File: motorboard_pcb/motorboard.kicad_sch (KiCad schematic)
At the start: 3 parts, among them U1 XIAO-RP2350-SMD, U3 ISO1640BQDRQ1, U4 LM5012QDDARQ1

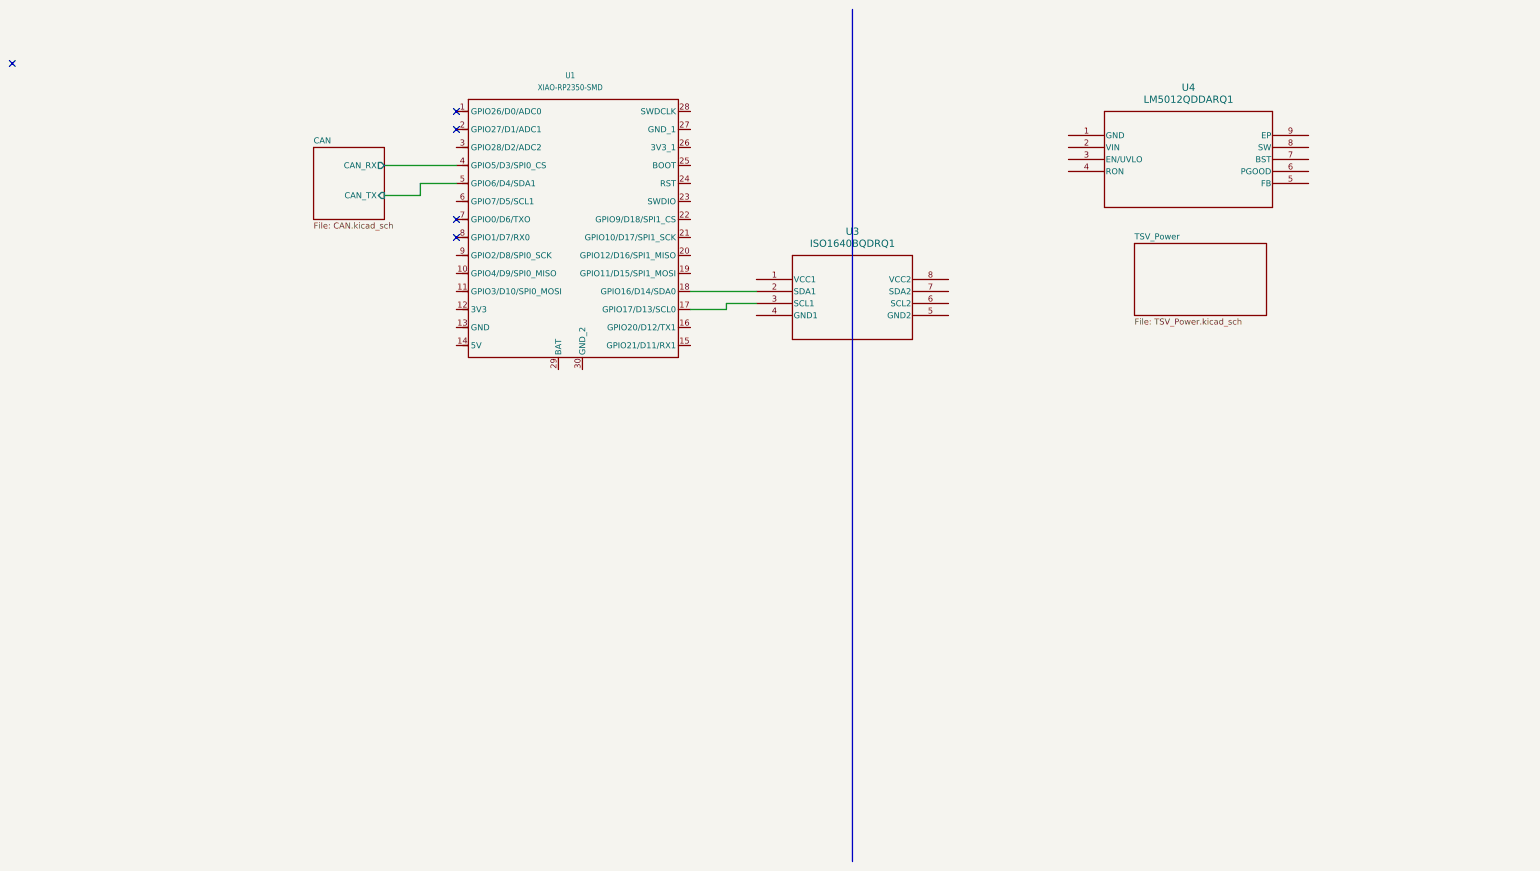
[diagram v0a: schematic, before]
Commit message: switch isolator for SPI, output stage (DAC, op amp)
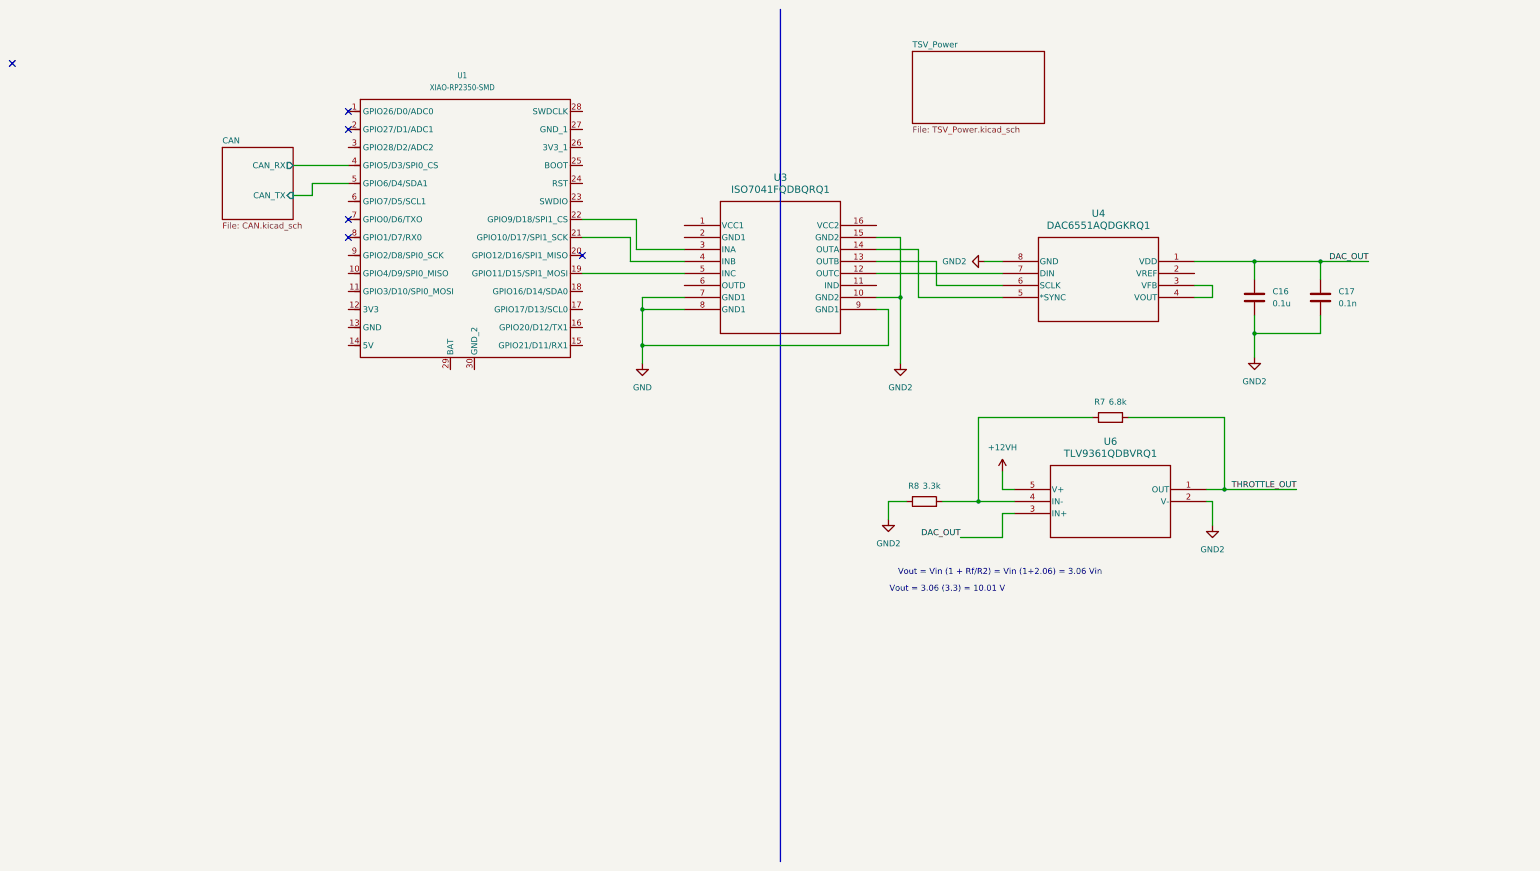
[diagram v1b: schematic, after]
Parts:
- removed U3: ISO1640BQDRQ1, ISO1640:SOIC8_D_TEX, symbol ISO1640:ISO1640BQDRQ1
- removed U4: LM5012QDDARQ1, SO-8-DDA_TEX, symbol 2025-02-28_21-05-36:LM5012QDDARQ1
- added C16: 0.1u, symbol Device:C
- added C17: 0.1n, symbol Device:C
- added R7: 6.8k, symbol Device:R
- added R8: 3.3k, symbol Device:R
- added U3: ISO7041FQDBQRQ1, SSOP16_DBQ_TEX, symbol ISO7041:ISO7041FQDBQRQ1
- added U4: DAC6551AQDGKRQ1, DGK8_TEX, symbol DAC6551:DAC6551AQDGKRQ1
- added U6: TLV9361QDBVRQ1, SOT23_DBV_TEX, symbol TLV9361:TLV9361QDBVRQ1
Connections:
- net at U1.19 (GPIO11/D15/SPI1_MOSI): now also U3.5 (INC)
- net at U1.21 (GPIO10/D17/SPI1_SCK): now also U3.4 (INB)
- net at U1.22 (GPIO9/D18/SPI1_CS): now also U3.3 (INA)
- new net: R7.1, R8.2, U6.4 (IN-)
- new net: U3.12 (OUTC), U4.7 (DIN)
- new net: U3.13 (OUTB), U4.6 (SCLK)
- new net: U3.14 (OUTA), U4.5 (*SYNC)
- new net: U4.3 (VFB), U4.4 (VOUT)
- new net +12VH: U6.5 (V+)
- new net DAC_OUT: C16.1, C17.1, U4.1 (VDD), U6.3 (IN+)
- new net GND: U3.7 (GND1), U3.8 (GND1), U3.9 (GND1)
- new net GND2: C16.2, C17.2, R8.1, U3.10 (GND2), U3.15 (GND2), U4.8 (GND), U6.2 (V-)
- new net THROTTLE_OUT: R7.2, U6.1 (OUT)
- no-connect marks 5 -> 6
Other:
- note added: "Vout = 3.06 (3.3) = 10.01 V"
- note added: "Vout = Vin (1 + Rf/R2) = Vin (1+2.06) = 3.06 Vin"
- moved on the sheet: U1

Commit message: Schematic done, pending review
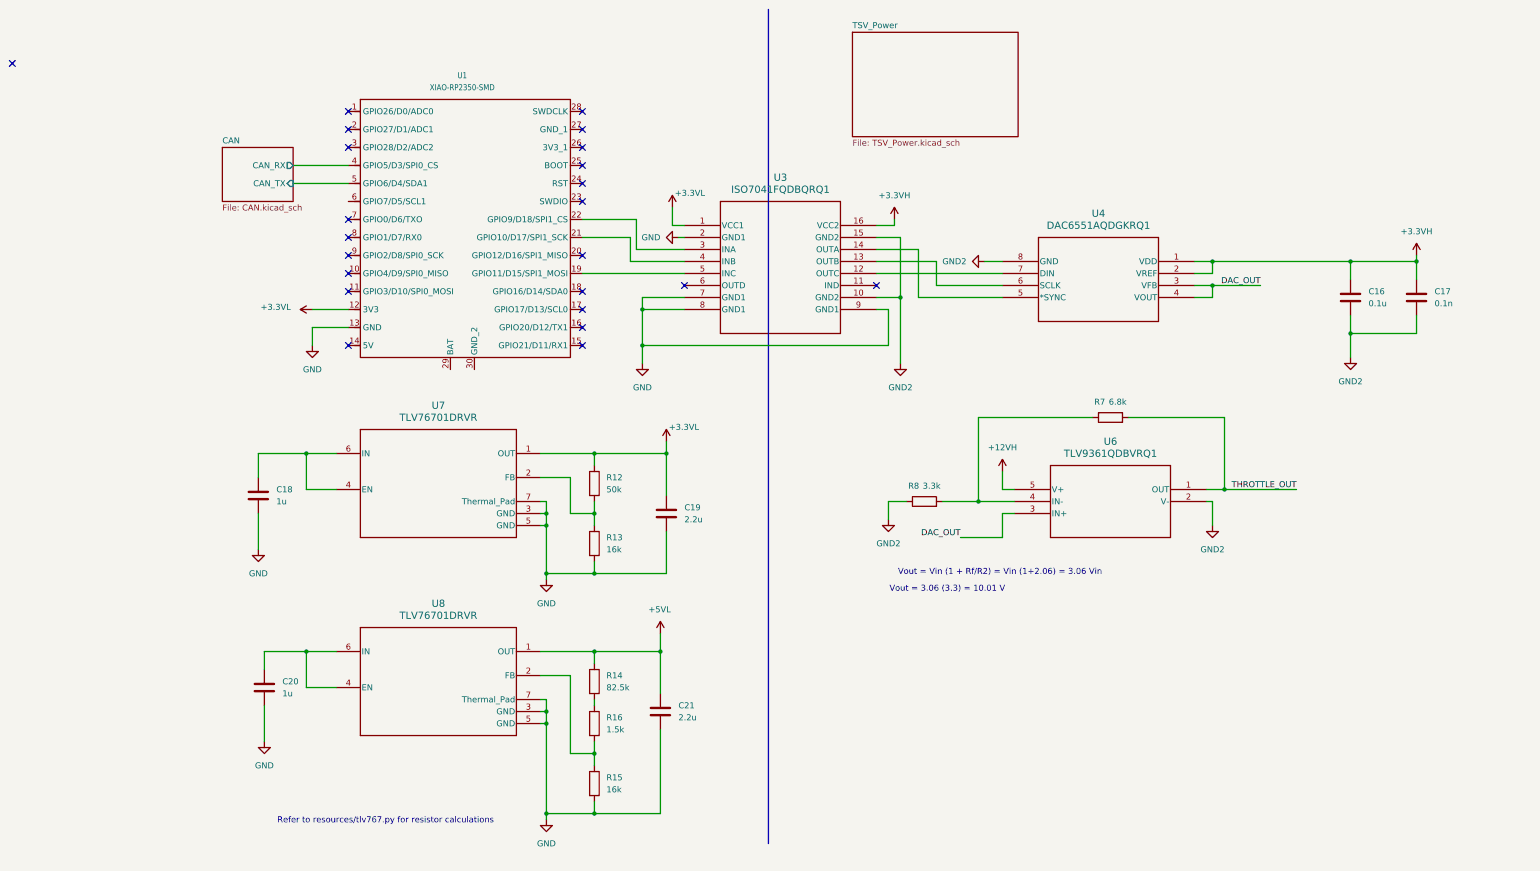
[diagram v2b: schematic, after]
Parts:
- added C18, C20: 1u, symbol Device:C
- added C19, C21: 2.2u, symbol Device:C
- added R12: 50k, symbol Device:R
- added R13, R15: 16k, symbol Device:R
- added R14: 82.5k, symbol Device:R
- added R16: 1.5k, symbol Device:R
- added U7, U8: TLV76701DRVR, TLV76701:DRV0006A-IPC_A, symbol TLV76701:TLV76701DRVR
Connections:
- net DAC_OUT: now also U4.3 (VFB), U4.4 (VOUT); no longer C16.1, C17.1, U4.1 (VDD)
- net GND: now also U1.13 (GND), U3.2 (GND1), C18.2, C19.2, C20.2, C21.2, R13.2, R15.2, U7.3 (GND), U7.5 (GND), U7.7 (Thermal_Pad), U8.3 (GND), U8.5 (GND), U8.7 (Thermal_Pad)
- net +3.3VL: now reaches U3.1 (VCC1)
- net +3.3VL: now also U1.12 (3V3), C19.1, R12.1, U7.1 (OUT)
- net +3.3VH: now reaches U3.16 (VCC2)
- net +3.3VH: now also C16.1, C17.1, U4.1 (VDD), U4.2 (VREF)
- new net: R15.1, R16.2, U8.2 (FB)
- new net: C20.1, U8.4 (EN), U8.6 (IN)
- new net: R12.2, R13.1, U7.2 (FB)
- new net: C18.1, U7.4 (EN), U7.6 (IN)
- new net: R14.2, R16.1
- new net +5VL: C21.1, R14.1, U8.1 (OUT)
- no-connect marks 6 -> 23
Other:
- note added: "Refer to resources/tlv767.py for resistor calculations"
- moved on the sheet: C16, C17

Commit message: Initial layout, all resistors/caps are 0602
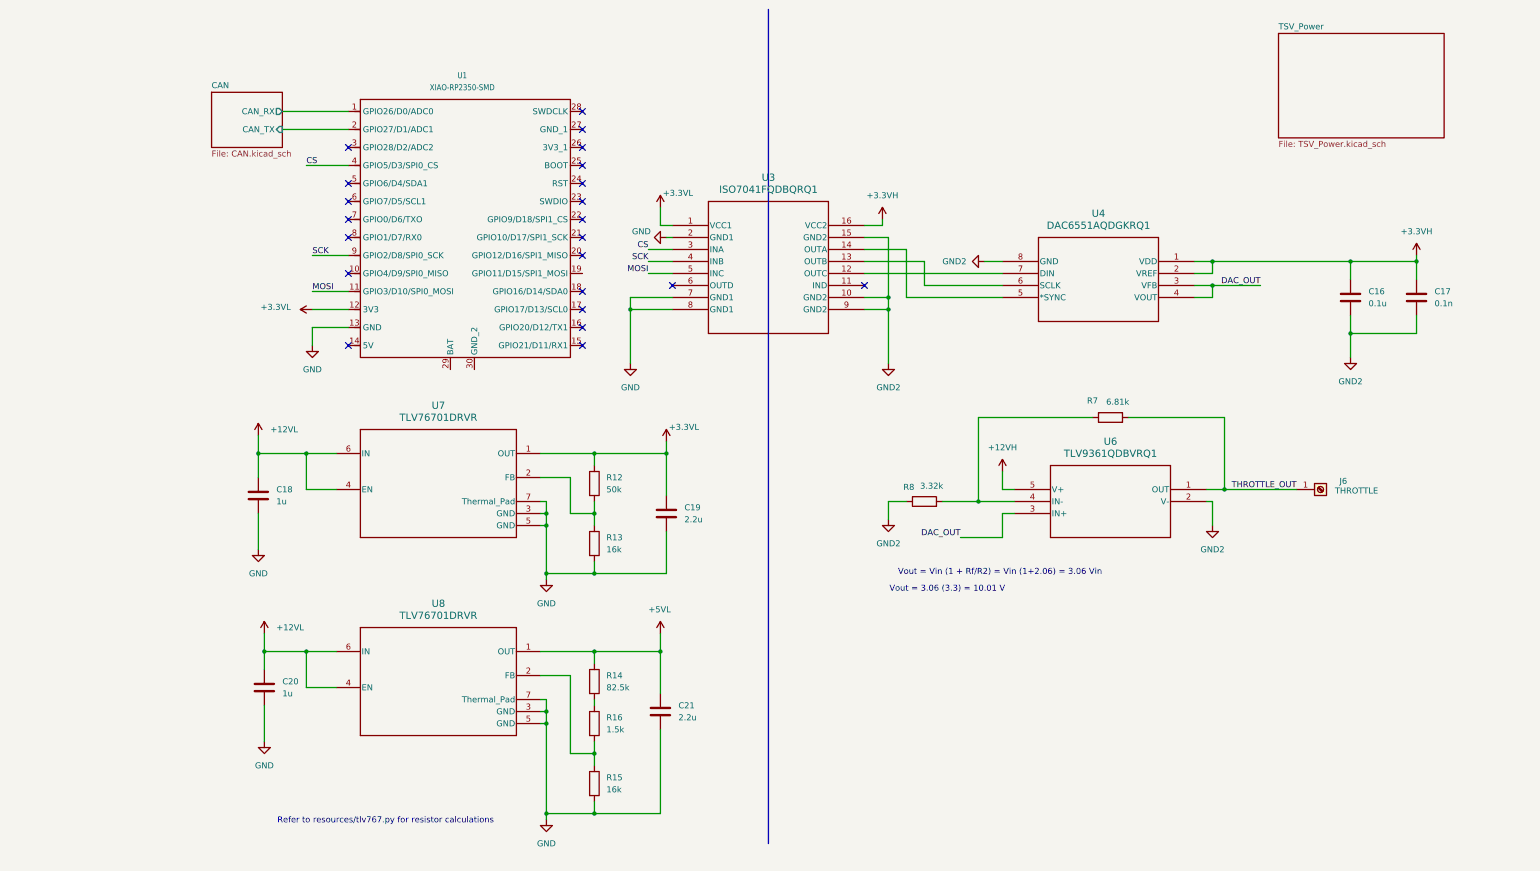
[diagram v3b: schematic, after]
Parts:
- added J6: THROTTLE, TerminalBlock_Wuerth:Wuerth_REDCUBE-THR_WP-THRBU_74650074_THR, symbol Connector:Screw_Terminal_01x01
- C16, C17, C18, C19, C20, C21: footprint (none) -> Capacitor_SMD:C_0603_1608Metric
- R12, R13, R14, R15, R16: footprint (none) -> Resistor_SMD:R_0603_1608Metric
- R7: value 6.8k -> 6.81k; footprint (none) -> Resistor_SMD:R_0603_1608Metric
- R8: value 3.3k -> 3.32k; footprint (none) -> Resistor_SMD:R_0603_1608Metric
- U3: footprint SSOP16_DBQ_TEX -> ISO7041:SSOP16_DBQ_TEX
- U4: footprint DGK8_TEX -> DAC6551:DGK8_TEX
- U6: footprint SOT23_DBV_TEX -> TLV9361QDBVRQ1:SOT23_DBV_TEX
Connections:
- net CAN/CAN_RX: now also U1.1 (GPIO26/D0/ADC0); no longer U1.4 (GPIO5/D3/SPI0_CS)
- net CAN/CAN_TX: now also U1.2 (GPIO27/D1/ADC1); no longer U1.5 (GPIO6/D4/SDA1)
- net GND: no longer U3.9 (GND1)
- net GND2: now also U3.9 (GND2)
- net THROTTLE_OUT: now also J6.1 (Pin_1)
- net +12VL: now reaches C20.1, U8.4 (EN), U8.6 (IN)
- net +12VL: now also C18.1, U7.4 (EN), U7.6 (IN)
- net at U1.22 (GPIO9/D18/SPI1_CS): no longer U3.3 (INA)
- net at U1.21 (GPIO10/D17/SPI1_SCK): no longer U3.4 (INB)
- net at U1.19 (GPIO11/D15/SPI1_MOSI): no longer U3.5 (INC)
- net MOSI: now reaches U1.11 (GPIO3/D10/SPI0_MOSI)
- net MOSI: now also U3.5 (INC)
- net SCK: now reaches U1.9 (GPIO2/D8/SPI0_SCK)
- net SCK: now also U3.4 (INB)
- new net CS: U1.4 (GPIO5/D3/SPI0_CS), U3.3 (INA)
- no-connect marks 23 -> 22
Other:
- moved on the sheet: U3

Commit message: layout finished, silkscreen finished, BOM finished
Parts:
- added H1, H2, H3, H4: MountingHole_Pad, MountingHole:MountingHole_2.2mm_M2, symbol Mechanical:MountingHole_Pad
- added L2: LQW15AN47NG00D, LQW15AN47NG00D:INDC1005X60N, symbol LQW15AN47NG00D:LQW15AN47NG00D
- R12: value 50k -> 49.9k
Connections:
- net +3.3VL: now also R12.2; no longer R12.1
- net +5VL: now also U1.14 (5V)
- net DAC_OUT: now also L2.2; no longer U4.3 (VFB), U4.4 (VOUT)
- net GND: now also H1.1, H2.1, H3.1, H4.1
- net at R13.1, U7.2 (FB): now also R12.1; no longer R12.2
- new net: L2.1, U4.3 (VFB), U4.4 (VOUT)
- no-connect marks 22 -> 23
